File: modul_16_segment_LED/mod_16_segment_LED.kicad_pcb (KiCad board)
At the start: 2 copper layers, 56.9 x 70.1 mm, 32 parts

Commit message: Перевёл проект на kicad 7.0 и внёс небольшие правки в обозначениях на схеме.
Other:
- net class Default removed

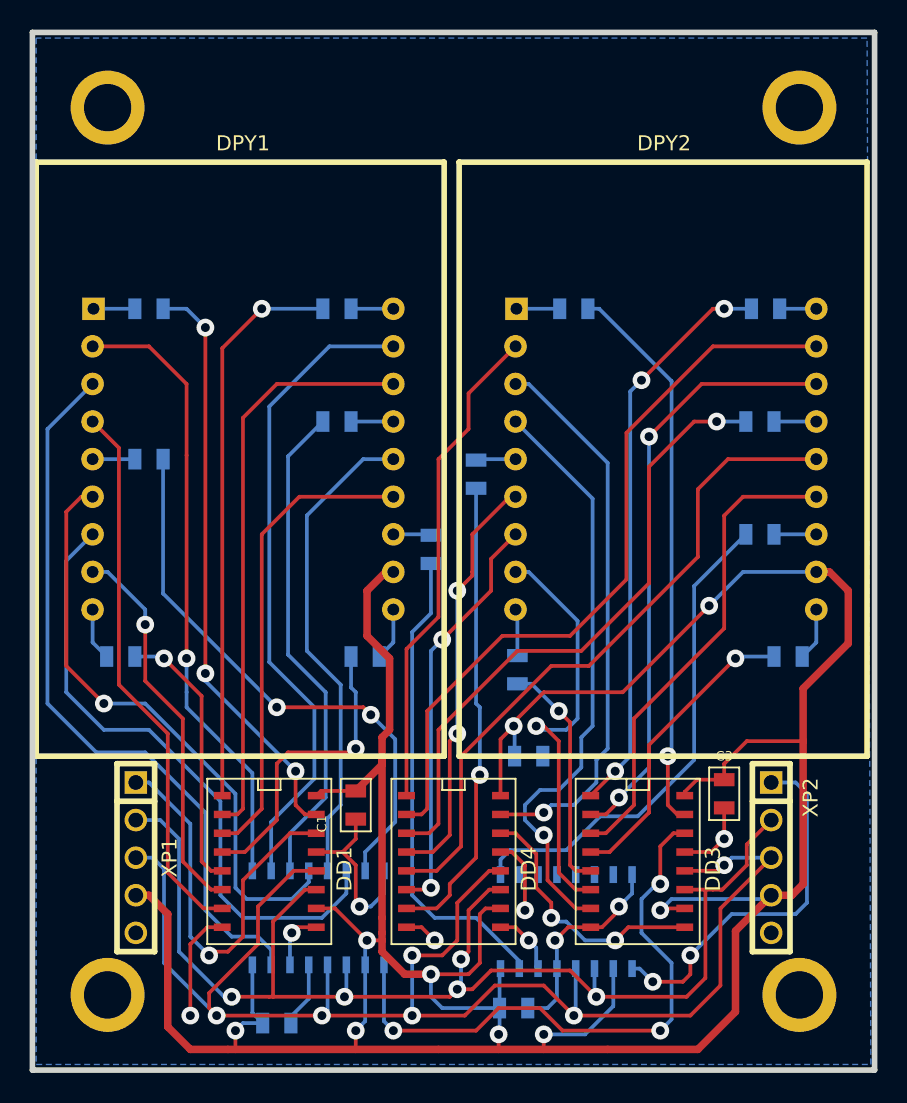
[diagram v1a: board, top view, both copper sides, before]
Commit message: Добавил дополнительные резисторы в схему16-ти сегментного индикатора.
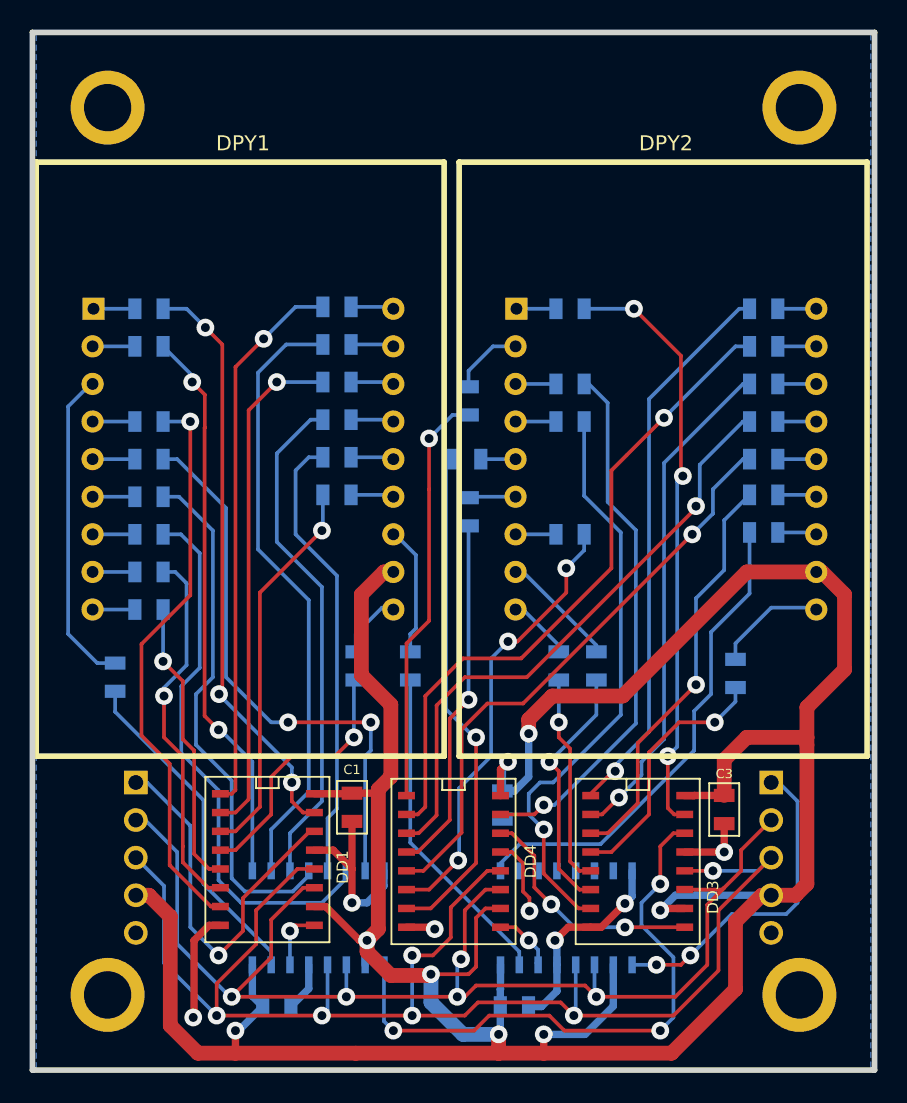
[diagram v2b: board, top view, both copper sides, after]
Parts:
- added R15: 220, IWsmd_case:SMD0805, B.Cu at (100.8, 108.2)
- added R16: 220, IWsmd_case:SMD0805, B.Cu at (100.8, 103.1)
- added R17: 220, IWsmd_case:SMD0805, B.Cu at (129.3, 93.0)
- added R18: 220, IWsmd_case:SMD0805, B.Cu at (142.4, 93.0)
- added R19: 220, IWsmd_case:SMD0805, B.Cu at (142.4, 98.0)
- added R20: 220, IWsmd_case:SMD0805, B.Cu at (142.4, 105.5)
- added R21: 220, IWsmd_case:SMD0805, B.Cu at (140.5, 117.6)
- added R22: 220, IWsmd_case:SMD0805, B.Cu at (128.5, 117.1)
- added R23: 220, IWsmd_case:SMD0805, B.Cu at (131.1, 117.1)
- added R24: 220, IWsmd_case:SMD0805, B.Cu at (129.3, 100.6)
- added R25: 220, IWsmd_case:SMD0805, B.Cu at (129.3, 98.0)
- added R26: 220, IWsmd_case:SMD0805, B.Cu at (122.4, 99.2)
- added R27: 220, IWsmd_case:SMD0805, B.Cu at (142.4, 95.5)
- added R28: 220, IWsmd_case:SMD0805, B.Cu at (142.4, 100.6)
- added R29: 220, IWsmd_case:SMD0805, B.Cu at (122.4, 106.7)
- added R30: 220, IWsmd_case:SMD0805, B.Cu at (142.4, 103.1)
- added R31: 220, IWsmd_case:SMD0805, B.Cu at (129.3, 108.2)
- added R32: 220, IWsmd_case:SMD0805, B.Cu at (122.3, 103.1)
- added R33: 220, IWsmd_case:SMD0805, B.Cu at (118.5, 117.1)
- added R34: 220, IWsmd_case:SMD0805, B.Cu at (142.4, 108.1)
- C1, C2, C3, C4, C5: value 0.1_мк -> 0.1 мк; footprint SMD0805 -> IWsmd_case:SMD0805
- DD1, DD2, DD3, DD4, DD5: value 74HC595B -> 74HC595D; footprint SOIC16 -> IWsmd_case:SOIC16
- DPY1, DPY2: footprint PSA12-11 -> IWcomponents:PSA12-11
- R1, R10, R11, R12, R13, R14, R2, R3, R4, R5, R6, R7, R8, R9: footprint SMD0805 -> IWsmd_case:SMD0805
- XP1: value PLS-5/PLS2-5R -> PLS-5/PLS-5R2; footprint PIN_ARRAY_5x1 -> IWconnectors:PIN_ARRAY_5x1; moved to B.Cu
- XP2: value PBS-5R -> PBS-5R2; footprint PIN_ARRAY_5x1 -> IWconnectors:PIN_ARRAY_5x1; moved to B.Cu
- moved R9 45.5 mm to (98.6, 117.9), turned to 90 degrees
- moved R8 42.3 mm to (100.8, 100.6), turned to 180 degrees
- moved R7 33.8 mm to (100.8, 110.7)
- moved R10 33.1 mm to (100.8, 95.5), turned to 180 degrees
- moved R11 29.0 mm to (113.5, 95.4)
- moved R14 29.0 mm to (113.5, 103.0)
- moved R13 19.4 mm to (100.8, 105.7), turned to 180 degrees
- moved R3 18.6 mm to (113.5, 97.9)
- moved R4 18.2 mm to (113.5, 105.5), turned to 0 degrees
- moved R5 16.6 mm to (114.8, 117.1), turned to 90 degrees
- moved R6 10.2 mm to (100.8, 113.3)
- moved R12 10.1 mm to (113.5, 100.5), turned to 0 degrees
- moved C4 3.75 mm to (124.7, 126.5), turned to 90 degrees
- moved C2 1.12 mm to (109.5, 140.1), turned to 180 degrees
- moved C3 1.07 mm to (139.7, 126.8), turned to 90 degrees
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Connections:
- C1 pad 1: /VCC -> /GND
- C1 pad 2: /GND -> /VCC
- C2 pad 1: /VCC -> /GND
- C2 pad 2: /GND -> /VCC
- C3 pad 1: /VCC -> /GND
- C3 pad 2: /GND -> /VCC
- C4 pad 1: /VCC -> /GND
- C4 pad 2: /GND -> /VCC
- C5 pad 1: /VCC -> /GND
- C5 pad 2: /GND -> /VCC
- DD1 pad 2: N-000036 -> Net-(DD1-Q2)
- DD1 pad 3: N-000043 -> Net-(DD1-Q3)
- DD1 pad 4: N-000054 -> Net-(DD1-Q4)
- DD1 pad 5: N-000056 -> Net-(DD1-Q5)
- DD1 pad 6: N-000045 -> Net-(DD1-Q6)
- DD1 pad 7: N-000047 -> Net-(DD1-Q7)
- DD2 pad 1: N-000049 -> Net-(DD2-Q1)
- DD2 pad 15: N-000060 -> Net-(DD2-Q0)
- DD2 pad 2: N-000035 -> Net-(DD2-Q2)
- DD2 pad 3: N-000034 -> Net-(DD2-Q3)
- DD2 pad 4: N-000057 -> Net-(DD2-Q4)
- DD2 pad 5: N-000033 -> Net-(DD2-Q5)
- DD2 pad 6: N-000046 -> Net-(DD2-Q6)
- DD2 pad 7: N-000040 -> Net-(DD2-Q7)
- DD3 pad 1: N-000024 -> Net-(DD3-Q1)
- DD3 pad 15: N-000041 -> Net-(DD3-Q0)
- DD3 pad 2: N-000009 -> Net-(DD3-Q2)
- DD3 pad 3: N-000008 -> Net-(DD3-Q3)
- DD3 pad 4: N-000026 -> Net-(DD3-Q4)
- DD3 pad 5: N-000028 -> Net-(DD3-Q5)
- DD3 pad 6: N-000007 -> Net-(DD3-Q6)
- DD3 pad 7: N-000006 -> Net-(DD3-Q7)
- DD4 pad 1: N-000004 -> Net-(DD4-Q1)
- DD4 pad 15: N-000030 -> Net-(DD4-Q0)
- DD4 pad 2: N-000012 -> Net-(DD4-Q2)
- DD4 pad 3: N-000014 -> Net-(DD4-Q3)
- DD4 pad 4: N-000003 -> Net-(DD4-Q4)
- DD4 pad 5: N-000001 -> Net-(DD4-Q5)
- DD4 pad 6: N-000002 -> Net-(DD4-Q6)
- DD4 pad 7: N-000062 -> Net-(DD4-Q7)
- DD5 pad 1: N-000048 -> Net-(DD5-Q1)
- DD5 pad 15: N-000015 -> Net-(DD5-Q0)
- DD5 pad 2: (no net) -> unconnected-(DD5-Q2-Pad2)
- DD5 pad 3: (no net) -> unconnected-(DD5-Q3-Pad3)
- DD5 pad 4: (no net) -> unconnected-(DD5-Q4-Pad4)
- DD5 pad 5: (no net) -> unconnected-(DD5-Q5-Pad5)
- DD5 pad 6: (no net) -> unconnected-(DD5-Q6-Pad6)
- DD5 pad 7: (no net) -> unconnected-(DD5-Q7-Pad7)
- DPY1 pad 10: N-000053 -> Net-(DPY1-e)
- DPY1 pad 12: N-000044 -> Net-(DPY1-DP)
- DPY1 pad 13: N-000043 -> Net-(DPY1-d)
- DPY1 pad 14: N-000033 -> Net-(DPY1-r)
- DPY1 pad 15: N-000038 -> Net-(DPY1-p)
- DPY1 pad 16: N-000036 -> Net-(DPY1-c)
- DPY1 pad 17: N-000035 -> Net-(DPY1-n)
- DPY1 pad 2: N-000049 -> Net-(DPY1-m)
- DPY1 pad 3: N-000060 -> Net-(DPY1-k)
- DPY1 pad 4: N-000047 -> Net-(DPY1-h)
- DPY1 pad 5: N-000058 -> Net-(DPY1-u)
- DPY1 pad 6: N-000057 -> Net-(DPY1-s)
- DPY1 pad 7: N-000046 -> Net-(DPY1-t)
- DPY1 pad 8: N-000045 -> Net-(DPY1-g)
- DPY1 pad 9: N-000055 -> Net-(DPY1-f)
- DPY2 pad 1: N-000005 -> Net-(DPY2-a)
- DPY2 pad 10: N-000025 -> Net-(DPY2-e)
- DPY2 pad 12: N-000011 -> Net-(DPY2-DP)
- DPY2 pad 13: N-000008 -> Net-(DPY2-d)
- DPY2 pad 14: N-000001 -> Net-(DPY2-r)
- DPY2 pad 15: N-000013 -> Net-(DPY2-p)
- DPY2 pad 16: N-000009 -> Net-(DPY2-c)
- DPY2 pad 17: N-000012 -> Net-(DPY2-n)
- DPY2 pad 18: N-000010 -> Net-(DPY2-b)
- DPY2 pad 2: N-000004 -> Net-(DPY2-m)
- DPY2 pad 3: N-000030 -> Net-(DPY2-k)
- DPY2 pad 4: N-000006 -> Net-(DPY2-h)
- DPY2 pad 5: N-000061 -> Net-(DPY2-u)
- DPY2 pad 6: N-000003 -> Net-(DPY2-s)
- DPY2 pad 7: N-000002 -> Net-(DPY2-t)
- DPY2 pad 8: N-000007 -> Net-(DPY2-g)
- DPY2 pad 9: N-000027 -> Net-(DPY2-f)
- R10 pad 1: N-000028 -> Net-(DD2-Q1)
- R10 pad 2: N-000027 -> Net-(DPY1-m)
- R11 pad 1: N-000014 -> Net-(DD2-Q2)
- R11 pad 2: N-000013 -> Net-(DPY1-n)
- R12 pad 1: N-000062 -> Net-(DD2-Q3)
- R12 pad 2: N-000061 -> Net-(DPY1-p)
- R13 pad 1: N-000015 -> Net-(DD2-Q4)
- R13 pad 2: N-000044 -> Net-(DPY1-s)
- R14 pad 1: N-000048 -> Net-(DD2-Q5)
- R14 pad 2: N-000011 -> Net-(DPY1-r)
- R3 pad 1: N-000054 -> Net-(DD1-Q2)
- R3 pad 2: N-000053 -> Net-(DPY1-c)
- R4 pad 1: N-000056 -> Net-(DD1-Q3)
- R4 pad 2: N-000055 -> Net-(DPY1-d)
- R5 pad 1: N-000034 -> Net-(DD1-Q4)
- R5 pad 2: N-000038 -> Net-(DPY1-e)
- R6 pad 1: N-000040 -> Net-(DD1-Q5)
- R6 pad 2: N-000058 -> Net-(DPY1-f)
- R7 pad 1: N-000041 -> Net-(DD1-Q6)
- R7 pad 2: N-000005 -> Net-(DPY1-g)
- R8 pad 1: N-000024 -> Net-(DD1-Q7)
- R8 pad 2: N-000010 -> Net-(DPY1-h)
- R9 pad 1: N-000026 -> Net-(DD2-Q0)
- R9 pad 2: N-000025 -> Net-(DPY1-k)
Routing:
- net N-000012: track 50.5 -> 0.00 mm
- net N-000060: track 49.7 -> 0.00 mm
- net N-000001: track 45.5 -> 0.00 mm
- net Net-(DD4-Q2): track 0.00 -> 44.5 mm, vias 0 -> 1
- net N-000035: track 43.9 -> 0.00 mm
- net N-000014: track 42.8 -> 0.00 mm, vias 1 -> 0
- net N-000046: track 42.6 -> 0.00 mm
- net N-000049: track 42.1 -> 0.00 mm, vias 1 -> 0
- net Net-(DD2-Q2): track 0.00 -> 41.3 mm
- net Net-(DD4-Q3): track 0.00 -> 40.6 mm, vias 0 -> 1
- net Net-(DD3-Q0): track 0.00 -> 40.6 mm, vias 0 -> 3
- net N-000009: track 40.5 -> 0.00 mm, vias 2 -> 0
- net N-000057: track 40.5 -> 0.00 mm, vias 1 -> 0
- net N-000006: track 40.3 -> 0.00 mm, vias 1 -> 0
- net Net-(DD4-Q5): track 0.00 -> 39.8 mm, vias 0 -> 1
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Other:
- board text added: "+5V"
- board text added: "CS"
- board text added: "DS"
- board text added: "GND"
- board text added: "SCK"

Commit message: Исправил на плате 16-ти сегментного индикатора размеры контуров платы и крепёжных отверстий.
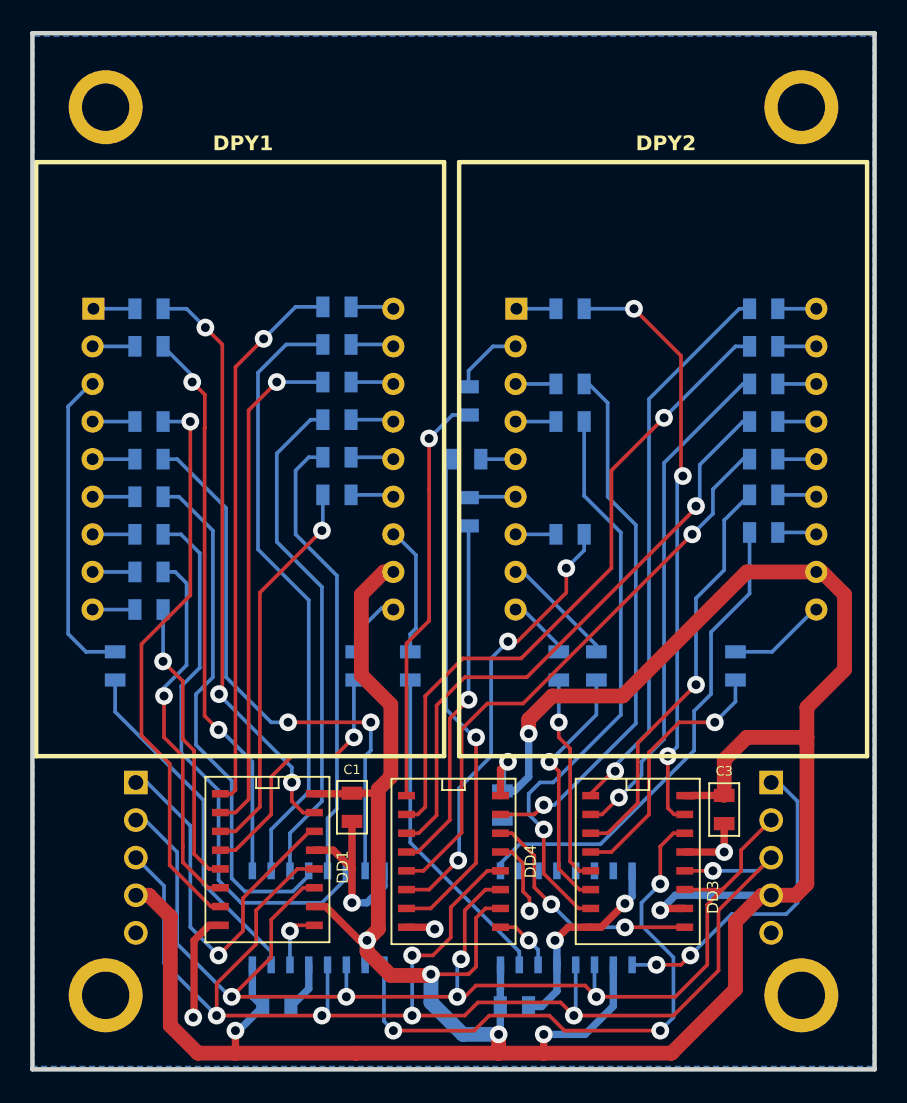
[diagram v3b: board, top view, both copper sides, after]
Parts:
- removed 1_PIN (x4): P***, 1_pin
- added PIN1: P***, IWconnectors:1_pin_3_2mm, F.Cu at (97.9, 79.3)
- added PIN2: P***, IWconnectors:1_pin_3_2mm, F.Cu at (144.9, 79.3)
- added PIN3: P***, IWconnectors:1_pin_3_2mm, F.Cu at (97.9, 139.3)
- added PIN4: P***, IWconnectors:1_pin_3_2mm, F.Cu at (144.9, 139.3)
- moved R9 0.76 mm to (98.6, 117.1)
- moved R21 0.51 mm to (140.5, 117.1)
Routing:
- net Net-(DPY2-e): track 7.54 -> 6.64 mm
- net Net-(DD2-Q0): track 22.8 -> 23.6 mm
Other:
- board size 56.9 x 70.1 mm -> 56.9 x 70 mm
- rule pad_to_mask_clearance: 0.254 -> 0.25
- board text added: "2x16 segment led display ver. 1.1"

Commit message: Подготовил печатные платы тензодатчика и 16-ти сегментного индикатора к отправке в производство.
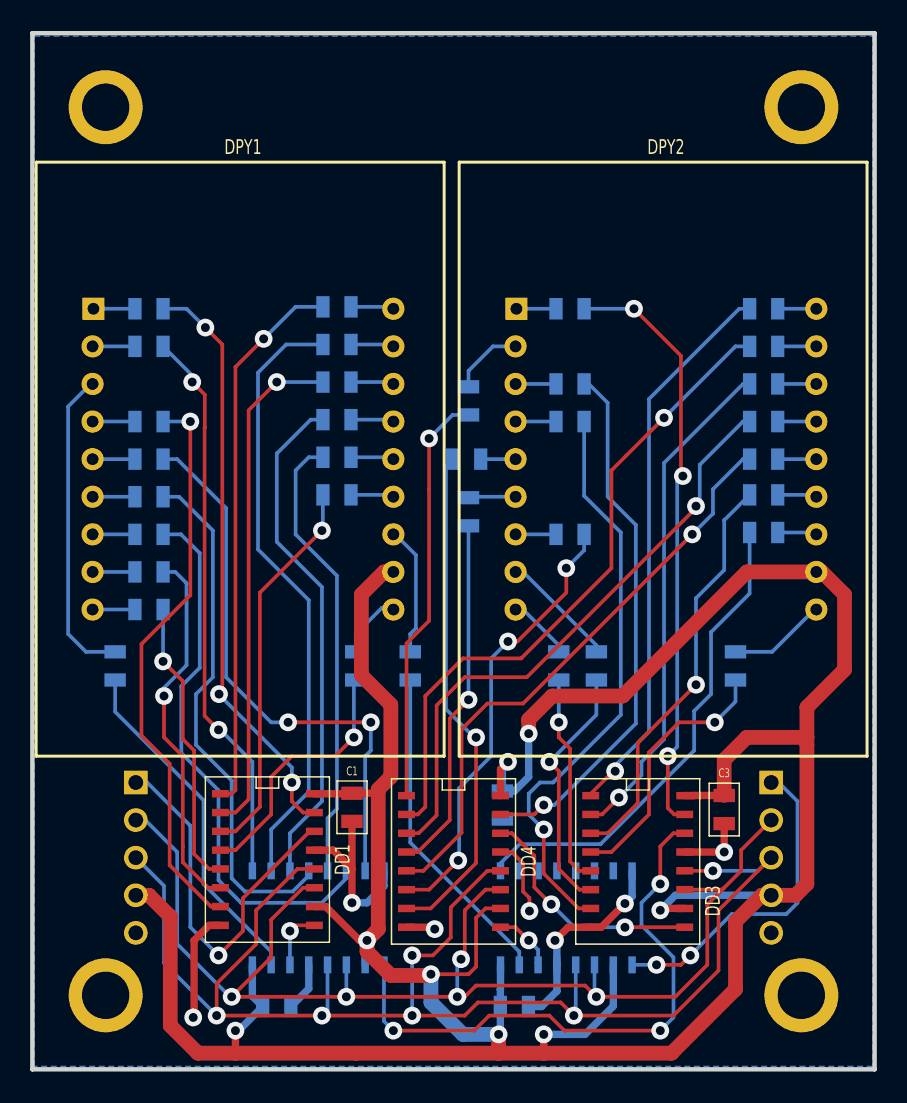
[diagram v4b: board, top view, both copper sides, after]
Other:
- rule pad_to_mask_clearance: 0.25 -> 0.2
